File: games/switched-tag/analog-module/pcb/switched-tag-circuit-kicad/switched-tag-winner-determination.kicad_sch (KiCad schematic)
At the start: 6 parts

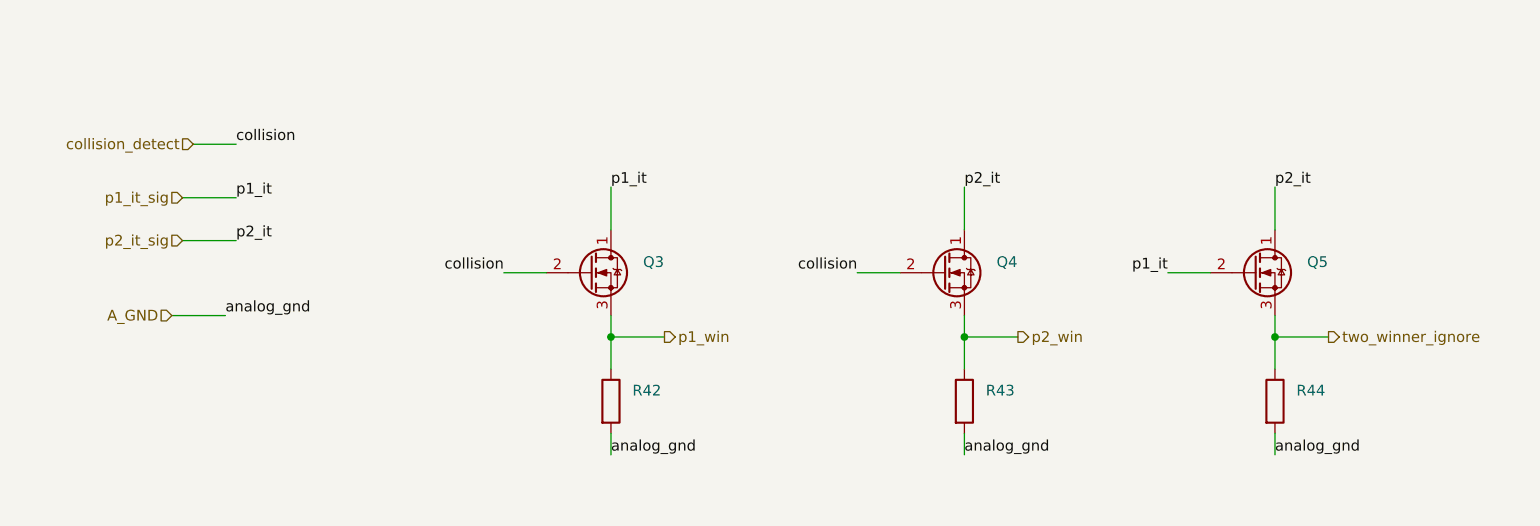
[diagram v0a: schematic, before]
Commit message: Converted Lm358.mod to .lib file for convenience.
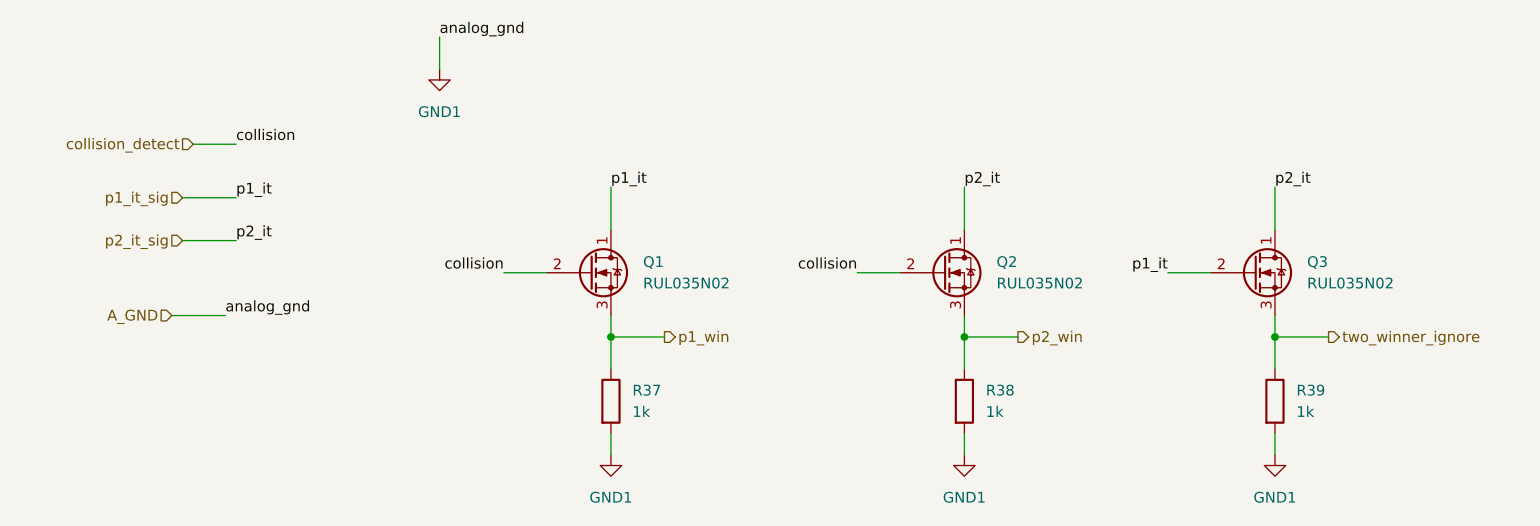
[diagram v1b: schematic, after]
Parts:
- Q1: renamed from Q3; value (none) -> RUL035N02; Spice_Lib_File ../../../../../spice-models/rul035n02.lib -> (none); Spice_Model RUL035N02 -> (none); Spice_Netlist_Enabled Y -> (none); Spice_Primitive X -> (none)
- Q2: renamed from Q4; value (none) -> RUL035N02; Spice_Lib_File ../../../../../spice-models/rul035n02.lib -> (none); Spice_Model RUL035N02 -> (none); Spice_Netlist_Enabled Y -> (none); Spice_Primitive X -> (none)
- Q3: renamed from Q5; value (none) -> RUL035N02; Spice_Lib_File ../../../../../spice-models/rul035n02.lib -> (none); Spice_Model RUL035N02 -> (none); Spice_Netlist_Enabled Y -> (none); Spice_Primitive X -> (none)
- R37: renamed from R42; value (none) -> 1k
- R38: renamed from R43; value (none) -> 1k
- R39: renamed from R44; value (none) -> 1k
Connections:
- net A_GND renamed GND1

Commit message: Updated simulation schematic. Need to fix timestep too small problem.
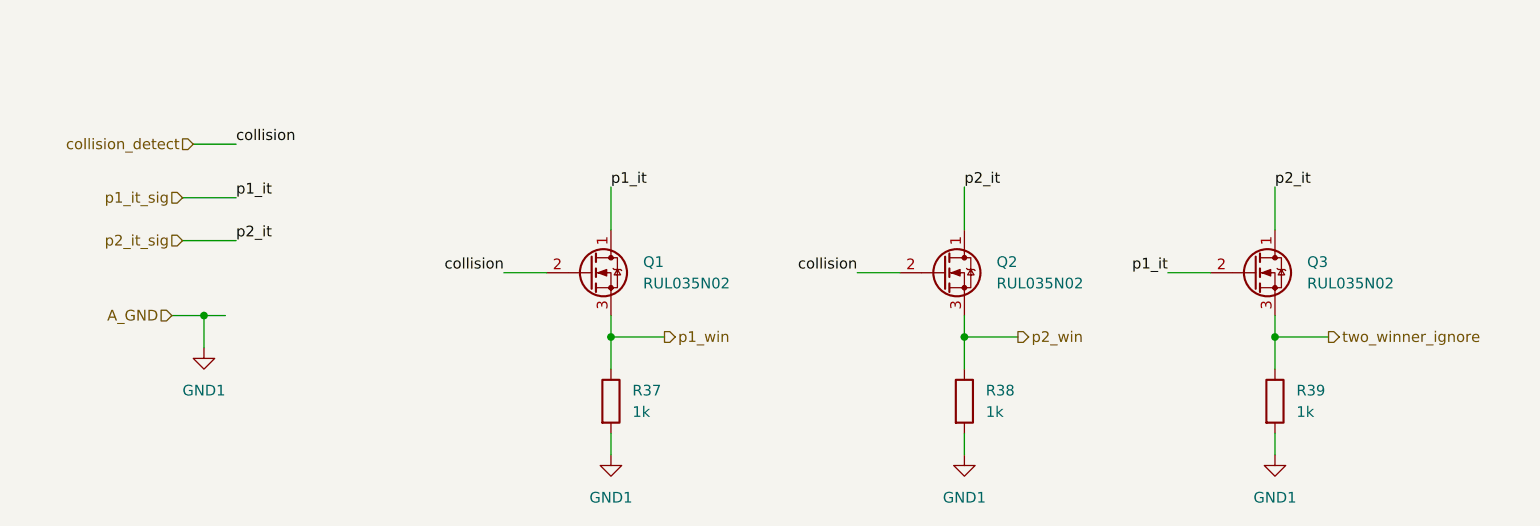
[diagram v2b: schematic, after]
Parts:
- R37, R38, R39: footprint (none) -> Resistor_SMD:R_0201_0603Metric
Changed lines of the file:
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@@
   (junction (at 156.21 114.3) (diameter 0) (color 0 0 0 0)
   )
+  (junction (at 66.04 111.76) (diameter 0) (color 0 0 0 0)
+  )
   (junction (at 193.04 114.3) (diameter 0) (color 0 0 0 0)
   )
   (junction (at 114.3 114.3) (diameter 0) (color 0 0 0 0)
   )
-  (wire (pts (xy 62.23 111.76) (xy 68.58 111.76))
+  (wire (pts (xy 66.04 111.76) (xy 68.58 111.76))
+    (stroke (width 0) (type default))
+  )
+  (wire (pts (xy 62.23 111.76) (xy 66.04 111.76))
     (stroke (width 0) (type default))
   )
@@
     (stroke (width 0) (type default))
   )
+  (wire (pts (xy 193.04 125.73) (xy 193.04 128.27))
+    (stroke (width 0) (type default))
+  )
   (wire (pts (xy 180.34 106.68) (xy 185.42 106.68))
     (stroke (width 0) (type default))
@@
     (stroke (width 0) (type default))
   )
-  (wire (pts (xy 93.98 78.74) (xy 93.98 82.55))
+  (wire (pts (xy 66.04 111.76) (xy 66.04 115.57))
     (stroke (width 0) (type default))
   )
@@
   )
   (wire (pts (xy 156.21 96.52) (xy 156.21 101.6))
-    (stroke (width 0) (type default))
-  )
-  (wire (pts (xy 193.04 125.73) (xy 193.04 128.27))
     (stroke (width 0) (type default))
   )
@@
     (effects (font (size 1.27 1.27)) (justify left bottom))
   )
-  (label "analog_gnd" (at 68.58 111.76 0) (fields_autoplaced)
-    (effects (font (size 1.27 1.27)) (justify left bottom))
-  )
-  (label "analog_gnd" (at 93.98 78.74 0) (fields_autoplaced)
-    (effects (font (size 1.27 1.27)) (justify left bottom))
-  )
   (hierarchical_label "p2_it_sig" (shape input) (at 63.5 102.87 180) (fields_autoplaced)
     (effects (font (size 1.27 1.27)) (justify right))
@@
       (effects (font (size 1.27 1.27)) (justify left))
     )
-    (property "Footprint" "" (at 112.522 121.92 90)
+    (property "Footprint" "Resistor_SMD:R_0201_0603Metric" (at 112.522 121.92 90)
       (effects (font (size 1.27 1.27)) hide)
     )
@@
   (symbol (lib_id "power:GND1") (at 114.3 128.27 0) (unit 1)
     (in_bom yes) (on_board yes) (dnp no) (fields_autoplaced)
-    (property "Reference" "#PWR061" (at 114.3 134.62 0)
+    (property "Reference" "#PWR063" (at 114.3 134.62 0)
       (effects (font (size 1.27 1.27)) hide)
     )
@@
       (project "switched-tag-circuit-kicad"
         (path "/e63e39d7-6ac0-4ffd-8aa3-1841a4541b55/5063b61c-13ff-4ac2-b013-ec01ef23a5a4"
-          (reference "#PWR061") (unit 1)
+          (reference "#PWR063") (unit 1)
         )
       )
@@
       (effects (font (size 1.27 1.27)) (justify left))
     )
-    (property "Footprint" "" (at 154.432 121.92 90)
+    (property "Footprint" "Resistor_SMD:R_0201_0603Metric" (at 154.432 121.92 90)
       (effects (font (size 1.27 1.27)) hide)
     )
@@
     )
   )
-  (symbol (lib_id "power:GND1") (at 93.98 82.55 0) (unit 1)
-    (in_bom yes) (on_board yes) (dnp no) (fields_autoplaced)
-    (property "Reference" "#PWR060" (at 93.98 88.9 0)
-      (effects (font (size 1.27 1.27)) hide)
-    )
-    (property "Value" "GND1" (at 93.98 87.63 0)
+  (symbol (lib_id "power:GND1") (at 66.04 115.57 0) (unit 1)
+    (in_bom yes) (on_board yes) (dnp no) (fields_autoplaced)
+    (property "Reference" "#PWR062" (at 66.04 121.92 0)
+      (effects (font (size 1.27 1.27)) hide)
+    )
+    (property "Value" "GND1" (at 66.04 120.65 0)
       (effects (font (size 1.27 1.27)))
     )
-    (property "Footprint" "" (at 93.98 82.55 0)
-      (effects (font (size 1.27 1.27)) hide)
-    )
-    (property "Datasheet" "" (at 93.98 82.55 0)
-      (effects (font (size 1.27 1.27)) hide)
-    )
-    (pin "1")
-    (instances
-      (project "switched-tag-circuit-kicad"
-        (path "/e63e39d7-6ac0-4ffd-8aa3-1841a4541b55/5063b61c-13ff-4ac2-b013-ec01ef23a5a4"
-          (reference "#PWR060") (unit 1)
+    (property "Footprint" "" (at 66.04 115.57 0)
+      (effects (font (size 1.27 1.27)) hide)
+    )
+    (property "Datasheet" "" (at 66.04 115.57 0)
+      (effects (font (size 1.27 1.27)) hide)
+    )
+    (pin "1")
+    (instances
+      (project "switched-tag-circuit-kicad"
+        (path "/e63e39d7-6ac0-4ffd-8aa3-1841a4541b55/5063b61c-13ff-4ac2-b013-ec01ef23a5a4"
+          (reference "#PWR062") (unit 1)
         )
       )
@@
       (effects (font (size 1.27 1.27)) hide)
     )
-    (property "Sim.Library" "../../../../../spice-models/rul035n02.lib" (at 111.76 106.68 0)
+    (property "Sim.Library" "${SPICE_MODEL_DIR_REL}/rul035n02.lib" (at 111.76 106.68 0)
       (effects (font (size 1.27 1.27)) hide)
     )
@@
       (effects (font (size 1.27 1.27)) (justify left))
     )
-    (property "Footprint" "" (at 191.262 121.92 90)
+    (property "Footprint" "Resistor_SMD:R_0201_0603Metric" (at 191.262 121.92 90)
       (effects (font (size 1.27 1.27)) hide)
     )
@@
   (symbol (lib_id "power:GND1") (at 193.04 128.27 0) (unit 1)
     (in_bom yes) (on_board yes) (dnp no) (fields_autoplaced)
-    (property "Reference" "#PWR063" (at 193.04 134.62 0)
+    (property "Reference" "#PWR065" (at 193.04 134.62 0)
       (effects (font (size 1.27 1.27)) hide)
     )
@@
       (project "switched-tag-circuit-kicad"
         (path "/e63e39d7-6ac0-4ffd-8aa3-1841a4541b55/5063b61c-13ff-4ac2-b013-ec01ef23a5a4"
-          (reference "#PWR063") (unit 1)
+          (reference "#PWR065") (unit 1)
         )
       )
@@
       (effects (font (size 1.27 1.27)) hide)
     )
-    (property "Sim.Library" "../../../../../spice-models/rul035n02.lib" (at 190.5 106.68 0)
+    (property "Sim.Library" "${SPICE_MODEL_DIR_REL}/rul035n02.lib" (at 190.5 106.68 0)
       (effects (font (size 1.27 1.27)) hide)
     )
@@
       (effects (font (size 1.27 1.27)) hide)
     )
-    (property "Sim.Library" "../../../../../spice-models/rul035n02.lib" (at 153.67 106.68 0)
+    (property "Sim.Library" "${SPICE_MODEL_DIR_REL}/rul035n02.lib" (at 153.67 106.68 0)
       (effects (font (size 1.27 1.27)) hide)
     )
@@
   (symbol (lib_id "power:GND1") (at 156.21 128.27 0) (unit 1)
     (in_bom yes) (on_board yes) (dnp no) (fields_autoplaced)
-    (property "Reference" "#PWR062" (at 156.21 134.62 0)
+    (property "Reference" "#PWR064" (at 156.21 134.62 0)
       (effects (font (size 1.27 1.27)) hide)
     )
@@
       (project "switched-tag-circuit-kicad"
         (path "/e63e39d7-6ac0-4ffd-8aa3-1841a4541b55/5063b61c-13ff-4ac2-b013-ec01ef23a5a4"
-          (reference "#PWR062") (unit 1)
-        )
-      )
+          (reference "#PWR064") (unit 1)
+        )
+      )

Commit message: Started pcb with placeholder components. Incomplete PCB.
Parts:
- Q1, Q2, Q3: footprint (none) -> Package_TO_SOT_SMD:SOT-89-5
- R37, R38, R39: footprint Resistor_SMD:R_0201_0603Metric -> Resistor_SMD:R_0603_1608Metric
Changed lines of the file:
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@@
       (effects (font (size 1.27 1.27)) (justify left))
     )
-    (property "Footprint" "Resistor_SMD:R_0201_0603Metric" (at 112.522 121.92 90)
+    (property "Footprint" "Resistor_SMD:R_0603_1608Metric" (at 112.522 121.92 90)
       (effects (font (size 1.27 1.27)) hide)
     )
@@
       (effects (font (size 1.27 1.27)) (justify left))
     )
-    (property "Footprint" "Resistor_SMD:R_0201_0603Metric" (at 154.432 121.92 90)
+    (property "Footprint" "Resistor_SMD:R_0603_1608Metric" (at 154.432 121.92 90)
       (effects (font (size 1.27 1.27)) hide)
     )
@@
       (effects (font (size 1.27 1.27)) (justify left))
     )
-    (property "Footprint" "" (at 116.84 104.14 0)
+    (property "Footprint" "Package_TO_SOT_SMD:SOT-89-5" (at 116.84 104.14 0)
       (effects (font (size 1.27 1.27)) hide)
     )
@@
       (effects (font (size 1.27 1.27)) (justify left))
     )
-    (property "Footprint" "Resistor_SMD:R_0201_0603Metric" (at 191.262 121.92 90)
+    (property "Footprint" "Resistor_SMD:R_0603_1608Metric" (at 191.262 121.92 90)
       (effects (font (size 1.27 1.27)) hide)
     )
@@
       (effects (font (size 1.27 1.27)) (justify left))
     )
-    (property "Footprint" "" (at 195.58 104.14 0)
+    (property "Footprint" "Package_TO_SOT_SMD:SOT-89-5" (at 195.58 104.14 0)
       (effects (font (size 1.27 1.27)) hide)
     )
@@
       (effects (font (size 1.27 1.27)) (justify left))
     )
-    (property "Footprint" "" (at 158.75 104.14 0)
-      (effects (font (size 1.27 1.27)) hide)
-    )
+    (property "Footprint" "Package_TO_SOT_SMD:SOT-89-5" (at 158.75 104.14 0)
+      (effects (font (size 1.27 1.27)) hide)
+    )

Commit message: Saving pcb placement.
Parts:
- removed Q3: RUL035N02, Package_TO_SOT_SMD:SOT-89-5, symbol Device:Q_NMOS_DGS
- removed R39: 1k, Resistor_SMD:R_0603_1608Metric, symbol Device:R
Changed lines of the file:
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@@
   (junction (at 66.04 111.76) (diameter 0) (color 0 0 0 0)
   )
-  (junction (at 193.04 114.3) (diameter 0) (color 0 0 0 0)
-  )
   (junction (at 114.3 114.3) (diameter 0) (color 0 0 0 0)
   )
@@
     (stroke (width 0) (type default))
   )
-  (wire (pts (xy 193.04 125.73) (xy 193.04 128.27))
-    (stroke (width 0) (type default))
-  )
-  (wire (pts (xy 180.34 106.68) (xy 185.42 106.68))
-    (stroke (width 0) (type default))
-  )
   (wire (pts (xy 114.3 111.76) (xy 114.3 114.3))
     (stroke (width 0) (type default))
@@
     (stroke (width 0) (type default))
   )
-  (wire (pts (xy 193.04 111.76) (xy 193.04 114.3))
-    (stroke (width 0) (type default))
-  )
   (wire (pts (xy 101.6 106.68) (xy 106.68 106.68))
     (stroke (width 0) (type default))
@@
     (stroke (width 0) (type default))
   )
-  (wire (pts (xy 193.04 114.3) (xy 193.04 118.11))
-    (stroke (width 0) (type default))
-  )
   (wire (pts (xy 64.77 91.44) (xy 69.85 91.44))
     (stroke (width 0) (type default))
   )
   (wire (pts (xy 156.21 114.3) (xy 162.56 114.3))
-    (stroke (width 0) (type default))
-  )
-  (wire (pts (xy 199.39 114.3) (xy 193.04 114.3))
-    (stroke (width 0) (type default))
-  )
-  (wire (pts (xy 193.04 96.52) (xy 193.04 101.6))
     (stroke (width 0) (type default))
   )
@@
     (effects (font (size 1.27 1.27)) (justify left bottom))
   )
-  (label "p1_it" (at 180.34 106.68 180) (fields_autoplaced)
-    (effects (font (size 1.27 1.27)) (justify right bottom))
-  )
   (label "p2_it" (at 156.21 96.52 0) (fields_autoplaced)
     (effects (font (size 1.27 1.27)) (justify left bottom))
   )
-  (label "p2_it" (at 193.04 96.52 0) (fields_autoplaced)
-    (effects (font (size 1.27 1.27)) (justify left bottom))
-  )
   (label "p1_it" (at 69.85 97.79 0) (fields_autoplaced)
     (effects (font (size 1.27 1.27)) (justify left bottom))
@@
   (hierarchical_label "A_GND" (shape input) (at 62.23 111.76 180) (fields_autoplaced)
     (effects (font (size 1.27 1.27)) (justify right))
-  )
-  (hierarchical_label "two_winner_ignore" (shape output) (at 199.39 114.3 0) (fields_autoplaced)
-    (effects (font (size 1.27 1.27)) (justify left))
   )
   (hierarchical_label "p2_win" (shape output) (at 162.56 114.3 0) (fields_autoplaced)
@@
         )
       )
-    )
-  )
-  (symbol (lib_id "Device:R") (at 193.04 121.92 0) (unit 1)
-    (in_bom yes) (on_board yes) (dnp no) (fields_autoplaced)
-    (property "Reference" "R39" (at 195.58 120.6499 0)
-      (effects (font (size 1.27 1.27)) (justify left))
-    )
-    (property "Value" "1k" (at 195.58 123.1899 0)
-      (effects (font (size 1.27 1.27)) (justify left))
-    )
-    (property "Footprint" "Resistor_SMD:R_0603_1608Metric" (at 191.262 121.92 90)
-      (effects (font (size 1.27 1.27)) hide)
-    )
-    (property "Datasheet" "~" (at 193.04 121.92 0)
-      (effects (font (size 1.27 1.27)) hide)
-    )
-    (pin "1")
-    (pin "2")
-    (instances
-      (project "switched-tag-circuit-kicad"
-        (path "/e63e39d7-6ac0-4ffd-8aa3-1841a4541b55/5063b61c-13ff-4ac2-b013-ec01ef23a5a4"
-          (reference "R39") (unit 1)
-        )
-      )
-    )
-  )
-  (symbol (lib_id "power:GND1") (at 193.04 128.27 0) (unit 1)
-    (in_bom yes) (on_board yes) (dnp no) (fields_autoplaced)
-    (property "Reference" "#PWR065" (at 193.04 134.62 0)
-      (effects (font (size 1.27 1.27)) hide)
-    )
-    (property "Value" "GND1" (at 193.04 133.35 0)
-      (effects (font (size 1.27 1.27)))
-    )
-    (property "Footprint" "" (at 193.04 128.27 0)
-      (effects (font (size 1.27 1.27)) hide)
-    )
-    (property "Datasheet" "" (at 193.04 128.27 0)
-      (effects (font (size 1.27 1.27)) hide)
-    )
-    (pin "1")
-    (instances
-      (project "switched-tag-circuit-kicad"
-        (path "/e63e39d7-6ac0-4ffd-8aa3-1841a4541b55/5063b61c-13ff-4ac2-b013-ec01ef23a5a4"
-          (reference "#PWR065") (unit 1)
-        )
-      )
-    )
-  )
-  (symbol (lib_id "Device:Q_NMOS_DGS") (at 190.5 106.68 0) (unit 1)
-    (in_bom yes) (on_board yes) (dnp no) (fields_autoplaced)
-    (property "Reference" "Q3" (at 196.85 105.4099 0)
-      (effects (font (size 1.27 1.27)) (justify left))
-    )
-    (property "Value" "RUL035N02" (at 196.85 107.9499 0)
-      (effects (font (size 1.27 1.27)) (justify left))
-    )
-    (property "Footprint" "Package_TO_SOT_SMD:SOT-89-5" (at 195.58 104.14 0)
-      (effects (font (size 1.27 1.27)) hide)
-    )
-    (property "Datasheet" "~" (at 190.5 106.68 0)
-      (effects (font (size 1.27 1.27)) hide)
-    )
-    (property "Sim.Library" "${SPICE_MODEL_DIR_REL}/rul035n02.lib" (at 190.5 106.68 0)
-      (effects (font (size 1.27 1.27)) hide)
-    )
-    (property "Sim.Name" "RUL035N02" (at 190.5 106.68 0)
-      (effects (font (size 1.27 1.27)) hide)
-    )
-    (property "Sim.Pins" "1=1 2=2 3=3" (at 0 0 0)
-      (effects (font (size 1.27 1.27)) hide)
-    )
-    (pin "1")
-    (pin "2")
-    (pin "3")
-    (instances
-      (project "switched-tag-circuit-kicad"
-        (path "/e63e39d7-6ac0-4ffd-8aa3-1841a4541b55/5063b61c-13ff-4ac2-b013-ec01ef23a5a4"
-          (reference "Q3") (unit 1)
-        )
-      )

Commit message: Changed component size from 0603 to 0805 for easier hand soldering.
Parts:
- R37, R38: footprint Resistor_SMD:R_0603_1608Metric -> Resistor_SMD:R_0805_2012Metric
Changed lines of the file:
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@@
       (effects (font (size 1.27 1.27)) (justify left))
     )
-    (property "Footprint" "Resistor_SMD:R_0603_1608Metric" (at 112.522 121.92 90)
+    (property "Footprint" "Resistor_SMD:R_0805_2012Metric" (at 112.522 121.92 90)
       (effects (font (size 1.27 1.27)) hide)
     )
@@
       (effects (font (size 1.27 1.27)) (justify left))
     )
-    (property "Footprint" "Resistor_SMD:R_0603_1608Metric" (at 154.432 121.92 90)
+    (property "Footprint" "Resistor_SMD:R_0805_2012Metric" (at 154.432 121.92 90)
       (effects (font (size 1.27 1.27)) hide)
     )
